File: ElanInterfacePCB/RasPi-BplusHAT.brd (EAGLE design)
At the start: 90 x 56 mm, 41 parts, among them K1 PIN20X2, Q1 220mA/50V/3.5Ω, Q10 1.1A/60V/600mΩ, Q12 1.1A/60V/600mΩ, Q13 220mA/50V/3.5Ω, Q2 1.1A/60V/600mΩ, Q3 220mA/50V/3.5Ω, Q4 1.1A/60V/600mΩ, Q5 220mA/50V/3.5Ω, Q6 1.1A/60V/600mΩ, Q7 220mA/50V/3.5Ω, Q8 1.1A/60V/600mΩ, Q9 220mA/50V/3.5Ω, U2 MAX481CUA+

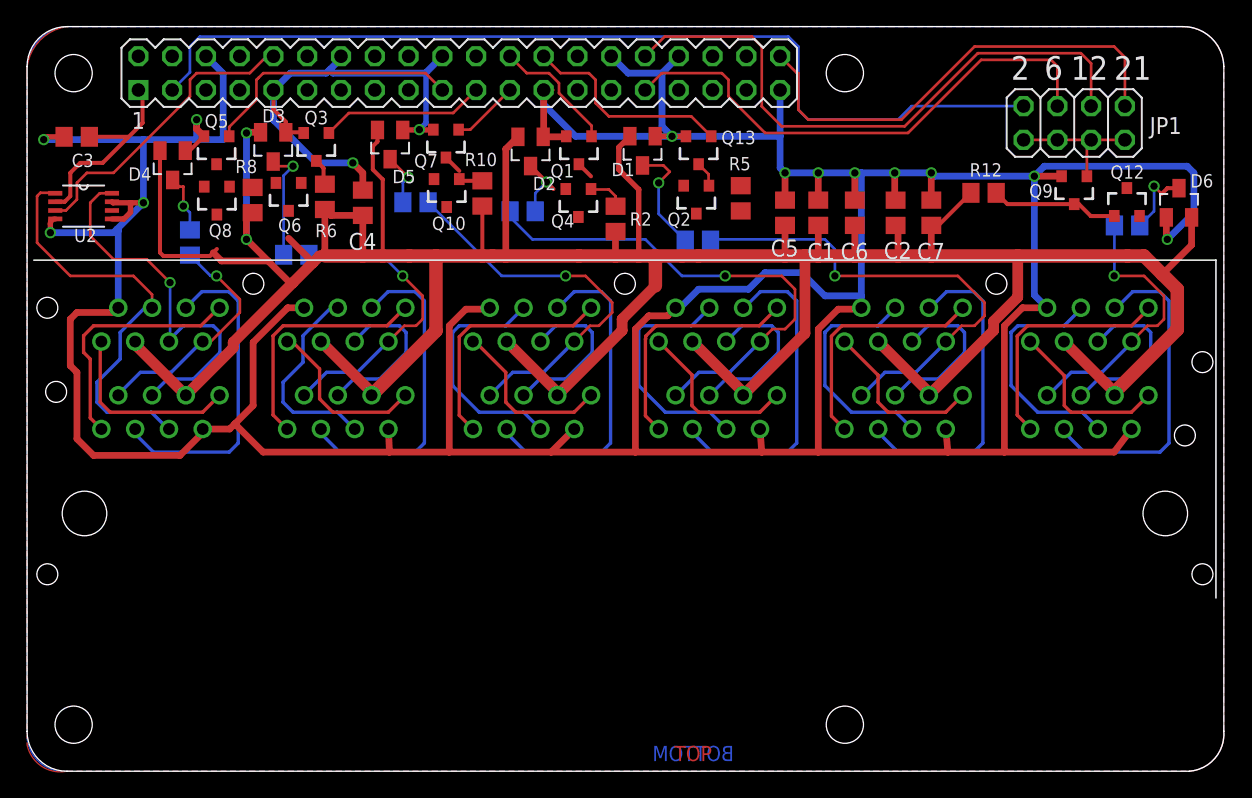
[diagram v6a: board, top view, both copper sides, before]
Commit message: Reworking Board smaller
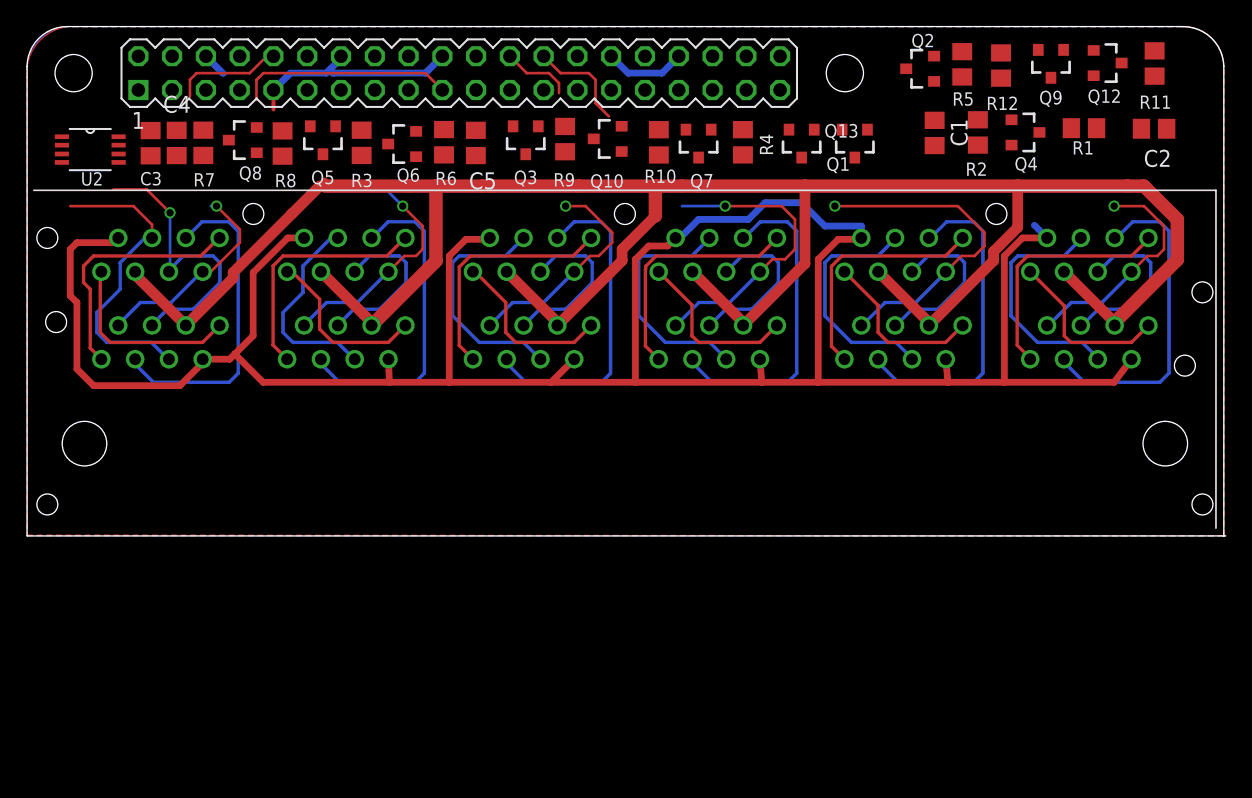
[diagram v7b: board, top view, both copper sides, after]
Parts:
- removed C6, C7: (no value), rcl:C0805
- removed D1, D2, D3, D4, D5, D6: BAS40-04, diode:SOT23
- removed JP1: (no value), pinhead:2X04
- moved R1 42.7 mm to (79.5, 48.4), flipped to the top
- moved Q4 34.0 mm to (75.0, 48.0), turned to 270 degrees
- moved R2 28.0 mm to (71.5, 48.0)
- moved C5 23.8 mm to (33.8, 47.2), turned to 270 degrees
- moved Q1 20.8 mm to (62.2, 47.2)
- moved C2 20.4 mm to (84.8, 48.3), turned to 180 degrees
- moved Q2 19.5 mm to (67.2, 52.8), turned to 90 degrees
- moved R5 19.5 mm to (70.3, 53.2), turned to 90 degrees
- moved Q7 19.0 mm to (50.5, 47.2)
- moved Q3 15.8 mm to (37.5, 47.5)
- moved C4 14.7 mm to (11.2, 47.2), turned to 270 degrees
- moved R10 13.8 mm to (47.5, 47.3), turned to 90 degrees
- moved Q10 12.8 mm to (43.7, 47.6), turned to 90 degrees
- moved R11 12.4 mm to (84.8, 53.2), flipped to the top, turned to 270 degrees
- moved R9 12.2 mm to (40.5, 47.5), flipped to the top, turned to 270 degrees
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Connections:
- removed net GPIOSEL: JP1.1, JP1.3, JP1.5, JP1.7, Q9.1
- new net GPIO6: Q9.1
- net +12V: no longer C6.1, C7.1, D1.2, D2.2, D3.2, D4.2, D5.2, D6.2
- net GND: no longer C6.2, C7.2, D1.1, D2.1, D3.1, D4.1, D5.1, D6.1
- net GPIO02: no longer JP1.2
- net GPIO06: no longer JP1.4
- net GPIO12: no longer JP1.6
- net GPIO21: no longer JP1.8
- net N$10: no longer D5.3
- net N$12: no longer D6.3
- net N$2: no longer D2.3
- net N$5: no longer D1.3
- net N$6: no longer D3.3
- net N$8: no longer D4.3
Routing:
- net GND: track 391.1 -> 211.1 mm, vias 14 -> 0
- net +12V: track 277.8 -> 177.2 mm, vias 2 -> 0
- net GPIO02: track 72.6 -> 0.00 mm
- net GPIO12: track 45.4 -> 0.00 mm
- net GPIO06: track 39.6 -> 0.00 mm
- net GPIO21: track 35.8 -> 0.00 mm
- net +3V3: track 15.6 -> 0.00 mm
- net ZONE4: track 37.8 -> 22.6 mm
- net RXI: track 22.7 -> 8.26 mm
- net ZONE3: track 29.5 -> 16.9 mm
- net GPIO09: track 13.0 -> 0.59 mm
- net ZONE5: track 36.6 -> 24.9 mm
- net GPIOSEL: track 10.6 -> 0.00 mm
- net N$11: track 9.60 -> 0.00 mm
- net N$6: track 8.67 -> 0.00 mm, vias 1 -> 0
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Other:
- board size 90 x 56 mm -> 90.2 x 38.3 mm
- board text removed: "12"
- board text removed: "2"
- board text removed: "21"
- board text removed: "6"
- board text removed: "BOTTOM"
- board text removed: "TOP"
